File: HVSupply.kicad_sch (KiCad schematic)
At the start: 9 parts, among them T1 Transformer_1P_1S, U5 L7812

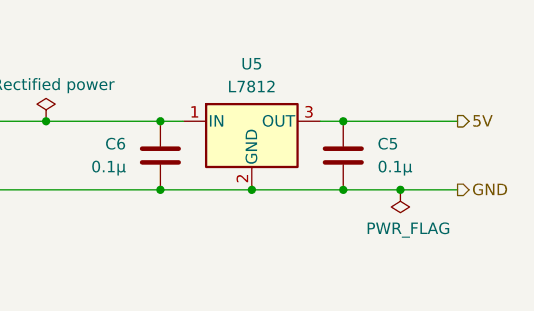
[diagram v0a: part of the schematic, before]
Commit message: update footprints, add 230v module, use SSRs and do some basic layouting
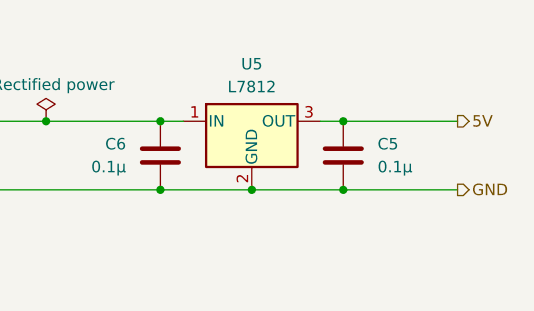
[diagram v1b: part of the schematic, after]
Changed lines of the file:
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@@
-	)
-	(junction
-		(at 173.99 115.57)
-		(diameter 0)
-		(color 0 0 0 0)
 	)
 	(junction
@@
 	(wire
 		(pts
-			(xy 167.64 115.57) (xy 173.99 115.57)
+			(xy 167.64 115.57) (xy 180.34 115.57)
 		)
 		(stroke
@@
 		(pts
 			(xy 120.65 115.57) (xy 147.32 115.57)
-		)
-		(stroke
-			(width 0)
-			(type default)
-		)
-	)
-	(wire
-		(pts
-			(xy 173.99 115.57) (xy 180.34 115.57)
 		)
 		(stroke
@@
 					(unit 1)
 				)
-			)
-		)
-	)
-	(symbol
-		(lib_id "power:PWR_FLAG")
-		(at 173.99 115.57 180)
-		(unit 1)
-		(exclude_from_sim no)
-		(in_bom yes)
-		(on_board yes)
-		(dnp no)
-		(property "Reference" "#FLG01"
-			(at 173.99 117.475 0)
-			(effects
-				(font
-					(size 1.27 1.27)
-				)
-				(hide yes)
-			)
-		)
-		(property "Value" "PWR_FLAG"
-			(at 170.18 119.888 0)
-			(effects
-				(font
-					(size 1.27 1.27)
-				)
-				(justify right)
-			)
-		)
-		(property "Footprint" ""
-			(at 173.99 115.57 0)
-			(effects
-				(font
-					(size 1.27 1.27)
-				)
-				(hide yes)
-			)
-		)
-		(property "Datasheet" "~"
-			(at 173.99 115.57 0)
-			(effects
-				(font
-					(size 1.27 1.27)
-				)
-				(hide yes)
-			)
-		)
-		(property "Description" "Special symbol for telling ERC where power comes from"
-			(at 173.99 115.57 0)
-			(effects
-				(font
-					(size 1.27 1.27)
-				)
-				(hide yes)
-			)
-		)
-		(pin "1"
-		)
-		(instances
-			(project "GaggiMate"
-				(path "/18f69721-6a2b-4a2b-8e72-291680dbbe9a/c32dc71d-382e-44f7-848c-34f69da70bf2"
-					(reference "#FLG01")
-					(unit 1)
-				)
